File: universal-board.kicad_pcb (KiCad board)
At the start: 2 copper layers, 61.2 x 77.5 mm, 49 parts, among them J1 USB_C_Receptacle, J2 Conn_02x04_Odd_Even, J3 Conn_01x08, J4 CONN_WS2812, J5 CONN_I2C_GROVE, Q1 BSS138, SW1 SW_RESET, SW2 SW_ACK, U1 USBLC6-2SC6, U2 AMS1117-3.3, U3 CH224K, U4 USBLC6-2SC6, U5 74AHCT1G125, U6 TSOP384xx, U7 ESP32-S3-WROOM-1

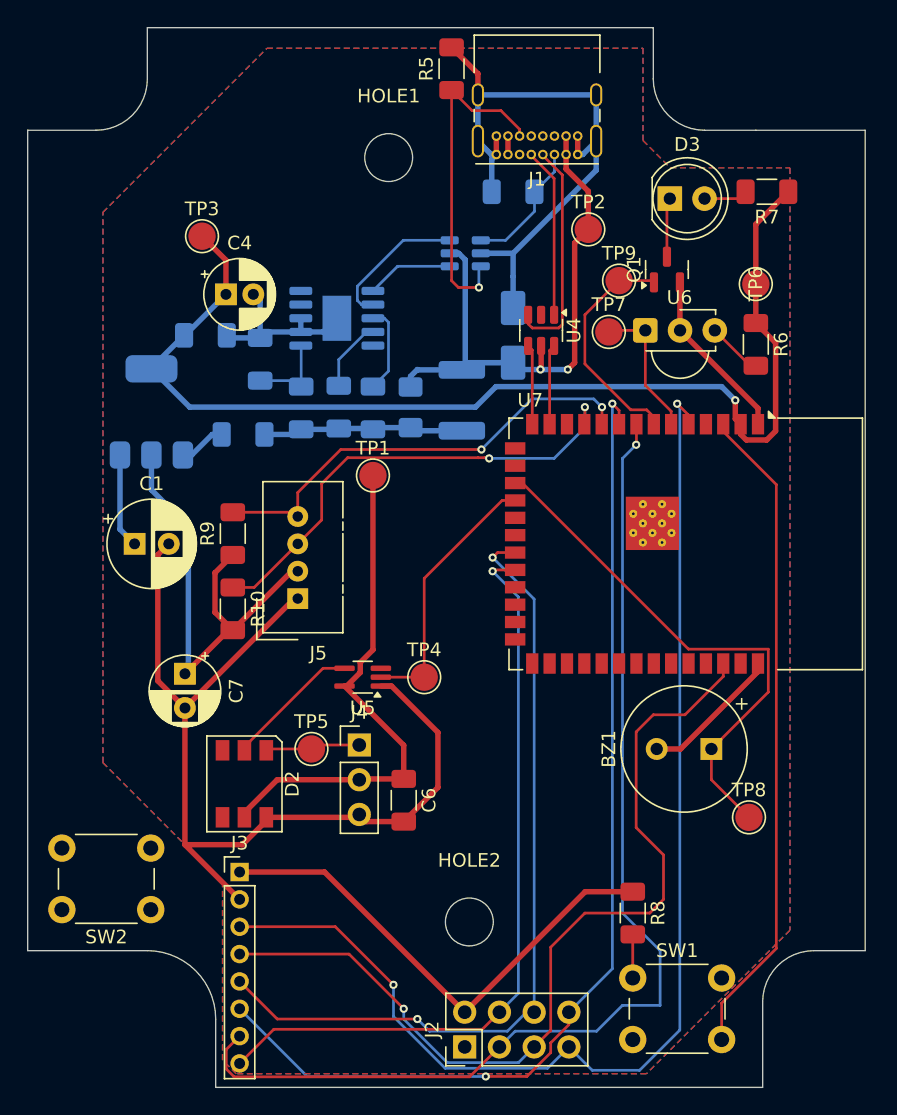
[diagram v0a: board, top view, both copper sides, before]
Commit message: DRC passes on schematic.
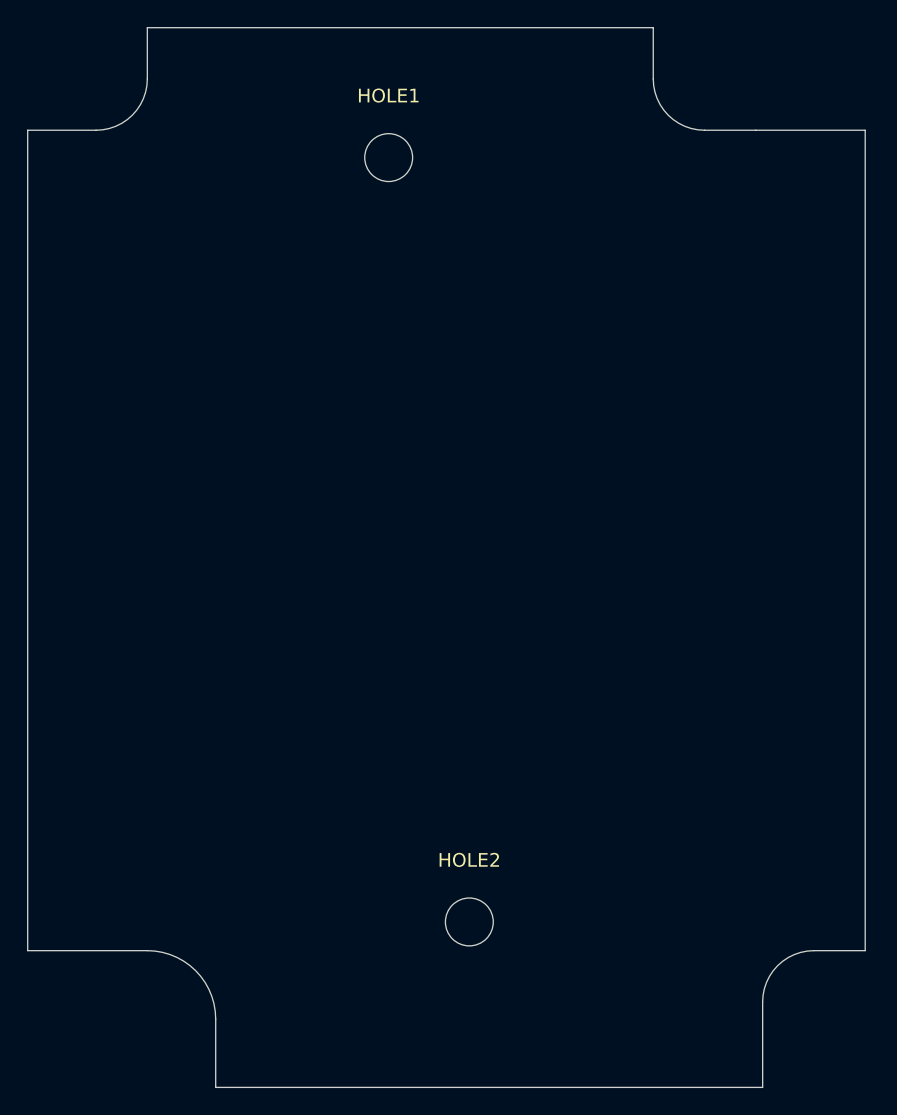
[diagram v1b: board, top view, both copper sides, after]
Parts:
- removed BZ1: LPT1440S-HS-05, Buzzer_Beeper:MagneticBuzzer_CUI_CST-931RP-A
- removed C1: 10uF, Capacitor_THT:CP_Radial_D6.3mm_P2.50mm
- removed C2, C3, C6: 100nF, Capacitor_SMD:C_1206_3216Metric_Pad1.33x1.80mm_HandSolder
- removed C4: 22uF, Capacitor_THT:CP_Radial_D5.0mm_P2.00mm
- removed C5: 1uF, Capacitor_SMD:C_1206_3216Metric_Pad1.33x1.80mm_HandSolder
- removed C7: 1uF, Capacitor_THT:CP_Radial_D5.0mm_P2.50mm
- removed D1: SMAJ5.0CA, Diode_SMD:D_SMA
- removed D2: WS2812, LED_SMD:LED_WS2812_PLCC6_5.0x5.0mm_P1.6mm
- removed D3: LL-503SIRC2H-1BE, LED_THT:LED_D5.0mm_Clear
- removed F1: PTS18126V300 (3A), Fuse:Fuse_1812_4532Metric_Pad1.30x3.40mm_HandSolder
- removed F2: 0ZCJ0100FF2E (1A), Fuse:Fuse_1206_3216Metric_Pad1.42x1.75mm_HandSolder
- removed J1: USB_C_Receptacle, Connector_USB:USB_C_Receptacle_GCT_USB4085
- removed J2: Conn_02x04_Odd_Even, Connector_PinHeader_2.54mm:PinHeader_2x04_P2.54mm_Vertical
- removed J3: Conn_01x08, Connector_PinHeader_2.00mm:PinHeader_1x08_P2.00mm_Vertical
- removed J4: CONN_WS2812, Connector_PinHeader_2.54mm:PinHeader_1x03_P2.54mm_Vertical
- removed J5: CONN_I2C_GROVE, Connector:NS-Tech_Grove_1x04_P2mm_Vertical
- removed Q1: BSS138, Package_TO_SOT_SMD:SOT-23
- removed R1, R3, R8: 10k, Capacitor_SMD:C_1206_3216Metric_Pad1.33x1.80mm_HandSolder
- removed R10, R9: 4.7k, Capacitor_SMD:C_1206_3216Metric_Pad1.33x1.80mm_HandSolder
- removed R2: 1k, Capacitor_SMD:C_1206_3216Metric_Pad1.33x1.80mm_HandSolder
- removed R4, R5: 5.1k, Capacitor_SMD:C_1206_3216Metric_Pad1.33x1.80mm_HandSolder
- removed R6: 100, Capacitor_SMD:C_1206_3216Metric_Pad1.33x1.80mm_HandSolder
- removed R7: 22, Capacitor_SMD:C_1206_3216Metric_Pad1.33x1.80mm_HandSolder
- removed SW1: SW_RESET, Button_Switch_THT:SW_PUSH_6mm
- removed SW2: SW_ACK, Button_Switch_THT:SW_PUSH_6mm
- removed TP1: TP_5V, TestPoint:TestPoint_Pad_D2.0mm
- removed TP2: TP_VBUS, TestPoint:TestPoint_Pad_D2.0mm
- removed TP3: TP_3.3V, TestPoint:TestPoint_Pad_D2.0mm
- removed TP4: TP_21812_3.3, TestPoint:TestPoint_Pad_D2.0mm
- removed TP5: TP_2812_5, TestPoint:TestPoint_Pad_D2.0mm
- removed TP6: TP_IR_TX_OUT, TestPoint:TestPoint_Pad_D2.0mm
- removed TP7: TP_IR_RX, TestPoint:TestPoint_Pad_D2.0mm
- removed TP8: TP_BUZZ, TestPoint:TestPoint_Pad_D2.0mm
- removed TP9: TP_IR_TX_IN, TestPoint:TestPoint_Pad_D2.0mm
- removed U1, U4: USBLC6-2SC6, Package_TO_SOT_SMD:SOT-23-6
- removed U2: AMS1117-3.3, Package_TO_SOT_SMD:SOT-223-3_TabPin2
- removed U3: CH224K, Package_SO:SSOP-10-1EP_3.9x4.9mm_P1mm_EP2.1x3.3mm
- removed U5: 74AHCT1G125, Package_TO_SOT_SMD:SOT-353_SC-70-5_Handsoldering
- removed U6: TSOP384xx, OptoDevice:Vishay_MINICAST-3Pin
- removed U7: ESP32-S3-WROOM-1, RF_Module:ESP32-S3-WROOM-1
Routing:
- net GND: track 157.9 -> 0.00 mm
- net 3.3V: track 154.6 -> 0.00 mm, vias 1 -> 0
- net MISO: track 88.1 -> 0.00 mm, vias 2 -> 0
- net GDO0: track 81.0 -> 0.00 mm, vias 1 -> 0
- net GDO2: track 76.6 -> 0.00 mm, vias 2 -> 0
- net SCK: track 65.5 -> 0.00 mm, vias 1 -> 0
- net 5V: track 60.7 -> 0.00 mm
- net MOSI: track 59.9 -> 0.00 mm, vias 2 -> 0
- net CSN: track 55.9 -> 0.00 mm, vias 1 -> 0
- net Net-(SW1-B): track 48.3 -> 0.00 mm
- net VBUS: track 46.6 -> 0.00 mm, vias 2 -> 0
- net BUZZ_IN: track 38.7 -> 0.00 mm
- net Net-(J5-Pin_3): track 35.0 -> 0.00 mm, vias 2 -> 0
- net Net-(J5-Pin_4): track 33.2 -> 0.00 mm, vias 2 -> 0
- net CC2: track 24.8 -> 0.00 mm, vias 1 -> 0
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- removed copper zone on B.Cu, net GND
- removed copper zone on F.Cu, net GND

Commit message: PCB is routed, but needs more work.
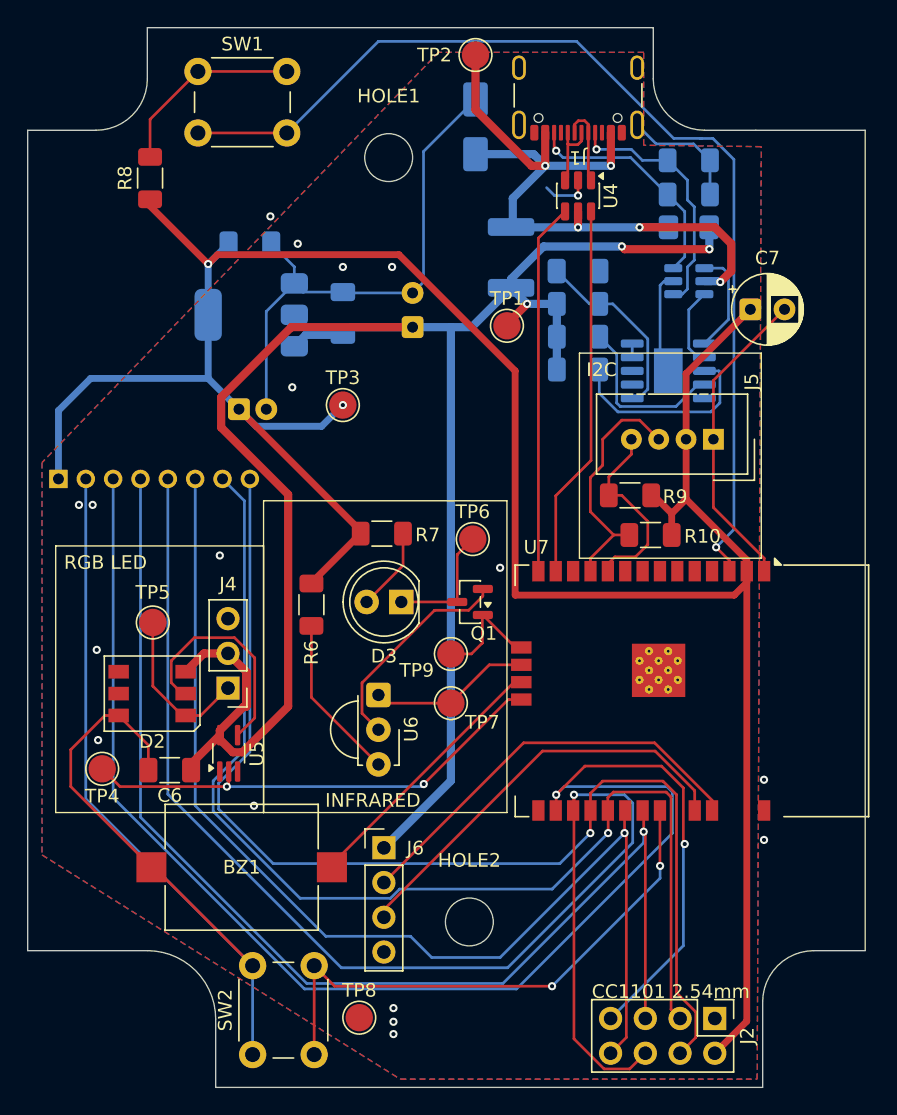
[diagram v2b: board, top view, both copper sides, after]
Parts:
- added BZ1: LPT1440S-HS-05, Buzzer_Beeper:Buzzer_Mallory_AST1109MLTRQ, F.Cu at (76.9, 131.4)
- added C1: 10uF, Capacitor_THT:CP_Radial_D6.3mm_P2.50mm, B.Cu at (89.4, 91.9)
- added C2: 100nF, Capacitor_SMD:C_1206_3216Metric_Pad1.33x1.80mm_HandSolder, B.Cu at (84.3, 90.9)
- added C3: 100nF, Capacitor_SMD:C_1206_3216Metric_Pad1.33x1.80mm_HandSolder, B.Cu at (77.5, 85.8)
- added C4: 22uF, Capacitor_THT:CP_Radial_D5.0mm_P2.00mm, B.Cu at (76.7, 97.9)
- added C5: 1uF, Capacitor_SMD:C_1206_3216Metric_Pad1.33x1.80mm_HandSolder, B.Cu at (101.5, 87.8)
- added C6: 100nF, Capacitor_SMD:C_1206_3216Metric_Pad1.33x1.80mm_HandSolder, F.Cu at (71.6, 124.3)
- added C7: 1uF, Capacitor_THT:CP_Radial_D5.0mm_P2.50mm, F.Cu at (114.1, 90.6)
- added D1: SMAJ5.0CA, Diode_SMD:D_SMA, B.Cu at (94.0, 77.2)
- added D2: WS2812, LED_SMD:LED_WS2812_PLCC6_5.0x5.0mm_P1.6mm, F.Cu at (70.3, 118.7)
- added D3: LL-503SIRC2H-1BE, LED_THT:LED_D5.0mm_Clear, F.Cu at (88.6, 112.0)
- added F1: PTS18126V300 (3A), Fuse:Fuse_1812_4532Metric_Pad1.30x3.40mm_HandSolder, B.Cu at (96.6, 86.8)
- added F2: 0ZCJ0100FF2E (1A), Fuse:Fuse_1206_3216Metric_Pad1.42x1.75mm_HandSolder, B.Cu at (109.6, 84.6)
- added J1: USB_C_Receptacle, Connector_USB:USB_C_Receptacle_GCT_USB4105-xx-A_16P_TopMnt_Horizontal, F.Cu at (101.5, 74.0)
- added J2: Conn_02x04_Odd_Even, Connector_PinHeader_2.54mm:PinHeader_2x04_P2.54mm_Vertical, F.Cu at (111.5, 142.5)
- added J3: Conn_01x08, Connector_PinHeader_2.00mm:PinHeader_1x08_P2.00mm_Vertical, B.Cu at (63.5, 103.0)
- added J4: CONN_WS2812, Connector_PinHeader_2.54mm:PinHeader_1x03_P2.54mm_Vertical, F.Cu at (75.9, 118.3)
- added J5: CONN_I2C_GROVE, Connector:NS-Tech_Grove_1x04_P2mm_Vertical, F.Cu at (111.4, 100.1)
- added J6: CONN_UART, Connector_PinHeader_2.54mm:PinHeader_1x04_P2.54mm_Vertical, F.Cu at (87.3, 130.0)
- added Q1: BSS138, Package_TO_SOT_SMD:SOT-23, F.Cu at (93.6, 112.0)
- added R1: 10k, Resistor_SMD:R_1206_3216Metric_Pad1.30x1.75mm_HandSolder, B.Cu at (101.5, 95.0)
- added R10: 4.7k, Resistor_SMD:R_1206_3216Metric_Pad1.30x1.75mm_HandSolder, F.Cu at (106.8, 107.1)
- added R2: 1k, Resistor_SMD:R_1206_3216Metric_Pad1.30x1.75mm_HandSolder, B.Cu at (101.5, 90.2)
- added R3: 10k, Resistor_SMD:R_1206_3216Metric_Pad1.30x1.75mm_HandSolder, B.Cu at (101.5, 92.6)
- added R4: 5.1k, Resistor_SMD:R_1206_3216Metric_Pad1.30x1.75mm_HandSolder, B.Cu at (109.6, 79.7)
- added R5: 5.1k, Resistor_SMD:R_1206_3216Metric_Pad1.30x1.75mm_HandSolder, B.Cu at (109.6, 82.2)
- added R6: 100, Resistor_SMD:R_1206_3216Metric_Pad1.30x1.75mm_HandSolder, F.Cu at (82.0, 112.2)
- added R7: 22, Resistor_SMD:R_1206_3216Metric_Pad1.30x1.75mm_HandSolder, F.Cu at (87.2, 107.0)
- added R8: 10k, Resistor_SMD:R_1206_3216Metric_Pad1.30x1.75mm_HandSolder, F.Cu at (70.2, 81.0)
- added R9: 4.7k, Resistor_SMD:R_1206_3216Metric_Pad1.30x1.75mm_HandSolder, F.Cu at (105.3, 104.2)
- added SW1: SW_RESET, Button_Switch_THT:SW_PUSH_6mm, F.Cu at (73.7, 73.2)
- added SW2: SW_ACK, Button_Switch_THT:SW_PUSH_6mm, F.Cu at (77.7, 145.1)
- added TP1: TP_5V, TestPoint:TestPoint_Pad_D2.0mm, F.Cu at (96.3, 91.8)
- added TP2: TP_VBUS, TestPoint:TestPoint_Pad_D2.0mm, F.Cu at (94.0, 72.0)
- added TP3: TP_3.3V, TestPoint:TestPoint_Pad_D2.0mm, F.Cu at (84.3, 97.6)
- added TP4: TP_21812_3.3, TestPoint:TestPoint_Pad_D2.0mm, F.Cu at (66.7, 124.2)
- added TP5: TP_2812_5, TestPoint:TestPoint_Pad_D2.0mm, F.Cu at (70.4, 113.5)
- added TP6: TP_IR_TX_OUT, TestPoint:TestPoint_Pad_D2.0mm, F.Cu at (93.8, 107.4)
- added TP7: TP_IR_RX, TestPoint:TestPoint_Pad_D2.0mm, F.Cu at (92.2, 119.4)
- added TP8: TP_BUZZ, TestPoint:TestPoint_Pad_D2.0mm, F.Cu at (85.5, 142.4)
- added TP9: TP_IR_TX_IN, TestPoint:TestPoint_Pad_D2.0mm, F.Cu at (92.2, 115.8)
- added U1: USBLC6-2SC6, Package_TO_SOT_SMD:SOT-23-6, B.Cu at (109.6, 88.5)
- added U2: AMS1117-3.3, Package_TO_SOT_SMD:SOT-223-3_TabPin2, B.Cu at (77.6, 91.0)
- added U3: CH224K, Package_SO:SSOP-10-1EP_3.9x4.9mm_P1mm_EP2.1x3.3mm, B.Cu at (108.1, 95.1)
- added U4: USBLC6-2SC6, Package_TO_SOT_SMD:SOT-23-6, F.Cu at (101.5, 82.3)
- added U5: 74AHCT1G125, Package_TO_SOT_SMD:SOT-353_SC-70-5_Handsoldering, F.Cu at (76.0, 123.1)
- added U6: TSOP384xx, OptoDevice:Vishay_MINICAST-3Pin, F.Cu at (86.9, 118.8)
- added U7: ESP32-S3-WROOM-1-N16, RF_Module:ESP32-S3-WROOM-1, F.Cu at (109.8, 118.5)
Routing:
- net 3.3V: track 0.00 -> 188.8 mm, vias 0 -> 2
- net GND: track 0.00 -> 175.6 mm, vias 0 -> 18
- net 5V: track 0.00 -> 151.2 mm, vias 0 -> 3
- net MISO: track 0.00 -> 117.7 mm, vias 0 -> 2
- net MOSI: track 0.00 -> 99.2 mm, vias 0 -> 1
- net SCK: track 0.00 -> 86.9 mm, vias 0 -> 1
- net CSN: track 0.00 -> 84.8 mm, vias 0 -> 1
- net GDO0: track 0.00 -> 83.4 mm, vias 0 -> 1
- net GDO2: track 0.00 -> 82.0 mm, vias 0 -> 1
- net Net-(SW1-B): track 0.00 -> 76.6 mm, vias 0 -> 1
- net VBUS: track 0.00 -> 55.4 mm, vias 0 -> 5
- net SW_ACK_OUT: track 0.00 -> 40.6 mm, vias 0 -> 2
- net WS2818_3.3V_IN: track 0.00 -> 35.0 mm, vias 0 -> 2
- net UART_RX: track 0.00 -> 30.7 mm
- net UART_TX: track 0.00 -> 30.7 mm
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- added copper zone on B.Cu, net GND
- added copper zone on F.Cu, net GND
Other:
- board text added: "1A PSU"
- board text added: "3A PSU"
- board text added: "5v -> 3.3v"
- board text added: "CC1101 2.54mm"
- board text added: "CC1101 2mm"
- board text added: "I2C"
- board text added: "INFRARED"
- board text added: "RGB LED"

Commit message: Rerouted PCB with freeroute. DRC still pending.
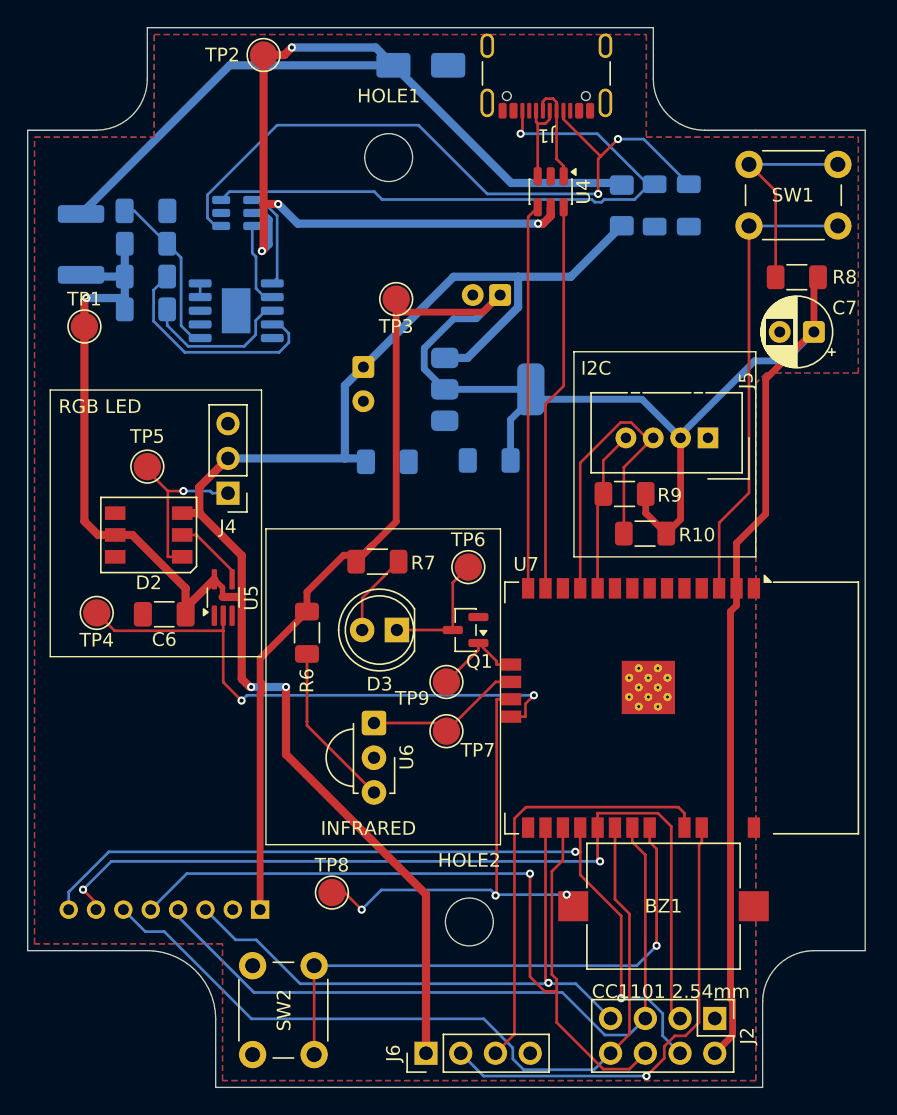
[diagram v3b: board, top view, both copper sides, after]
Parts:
- moved R8 47.9 mm to (117.5, 88.2), turned to 180 degrees
- moved SW1 40.9 mm to (114.0, 80.0)
- moved J3 34.8 mm to (78.2, 134.5), turned to 90 degrees
- moved U1 33.4 mm to (76.5, 83.5)
- moved C5 31.9 mm to (69.9, 83.4)
- moved R1 31.9 mm to (69.9, 90.6)
- moved R2 31.9 mm to (69.9, 85.8)
- moved R3 31.9 mm to (69.9, 88.2)
- moved U3 31.9 mm to (76.5, 90.7)
- moved F1 31.5 mm to (65.2, 85.8)
- moved BZ1 31.0 mm to (107.8, 134.2), turned to 0 degrees
- moved TP1 30.9 mm to (65.4, 91.8)
- moved C3 23.6 mm to (95.0, 101.7), turned to 180 degrees
- moved C4 20.8 mm to (95.8, 89.5), turned to 180 degrees
- moved U2 18.1 mm to (94.9, 96.5), turned to 0 degrees
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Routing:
- net GND: track 175.6 -> 0.00 mm, vias 18 -> 0
- net MISO: track 117.7 -> 44.4 mm, vias 2 -> 1
- net VBUS: track 55.4 -> 98.7 mm, vias 5 -> 4
- net Net-(SW1-B): track 76.6 -> 33.9 mm, vias 1 -> 0
- net MOSI: track 99.2 -> 61.9 mm
- net SCK: track 86.9 -> 53.1 mm, vias 1 -> 0
- net CC1: track 18.4 -> 51.3 mm, vias 1 -> 2
- net CC2: track 17.1 -> 45.5 mm
- net CSN: track 84.8 -> 60.6 mm, vias 1 -> 2
- net GDO2: track 82.0 -> 59.0 mm, vias 1 -> 0
- net GDO0: track 83.4 -> 64.2 mm, vias 1 -> 2
- net BUZZ_IN: track 19.6 -> 35.0 mm, vias 0 -> 3
- net Net-(D2-DIN): track 16.6 -> 5.37 mm
- net 3.3V: track 188.8 -> 178.5 mm, vias 2 -> 0
- net Net-(J5-Pin_3): track 17.8 -> 23.9 mm
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
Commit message: revision 1 - off to manufacturing
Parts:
- moved J1 1.93 mm to (99.2, 74.3)
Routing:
- net CC2: track 45.5 -> 38.5 mm
- net 5V: track 148.5 -> 153.0 mm
- net 3.3V: track 178.5 -> 181.6 mm
- net Net-(J1-D--PadA7): track 7.50 -> 5.57 mm
- net CC1: track 51.3 -> 49.5 mm
- net GND: vias 0 -> 8
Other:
- board text added: "github.com/jasiek/esphome-universal-board"
- board text added: "rev 1"
